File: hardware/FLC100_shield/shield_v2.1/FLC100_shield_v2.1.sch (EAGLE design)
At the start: 55 parts, among them IC2 TSR 1-2450, Q1 2N7000, Q2 2N7000, Q3 2N7000, Q4 2N7000, Q5 2N7000, Q6 2N7000, Q7 2N7000, Q8 2N7000, Q9 2N7000, X1 RJ45, X2 RJ11, X3 CLOUD SENSOR, X4 MEGA2560, X5 HUMIDITY

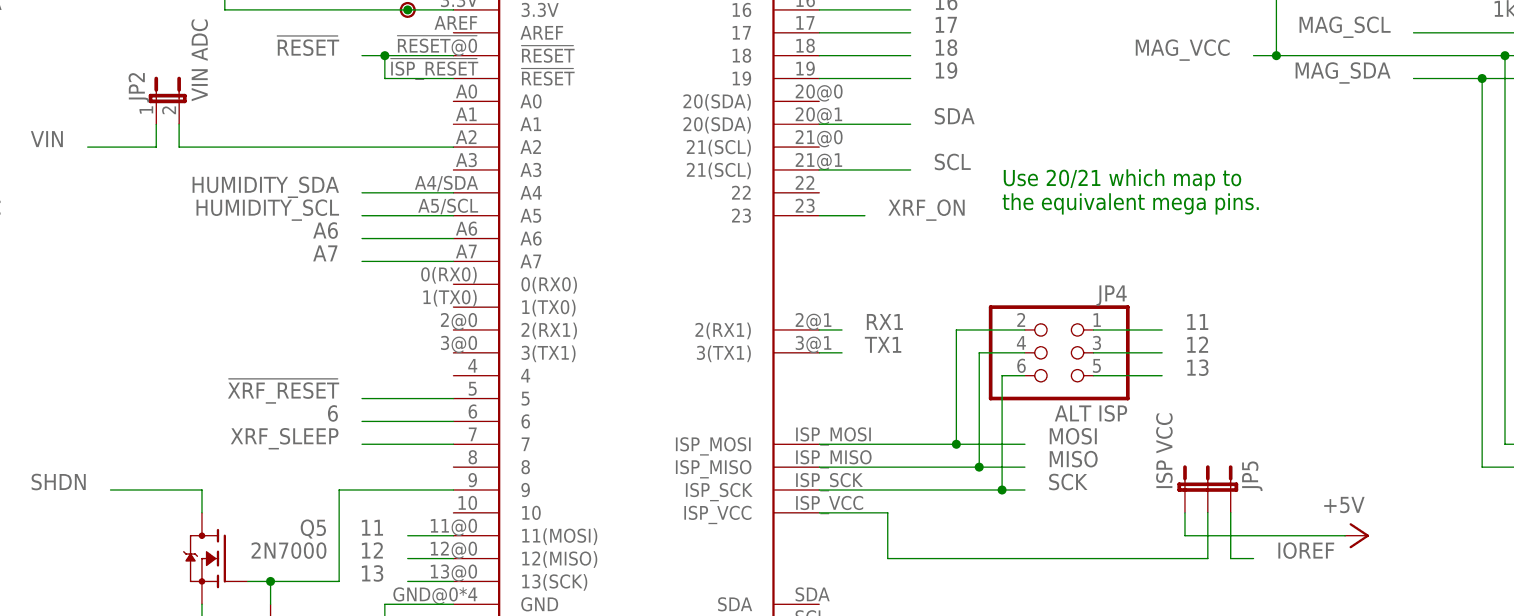
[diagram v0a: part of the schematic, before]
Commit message: Remove unused XRF nets
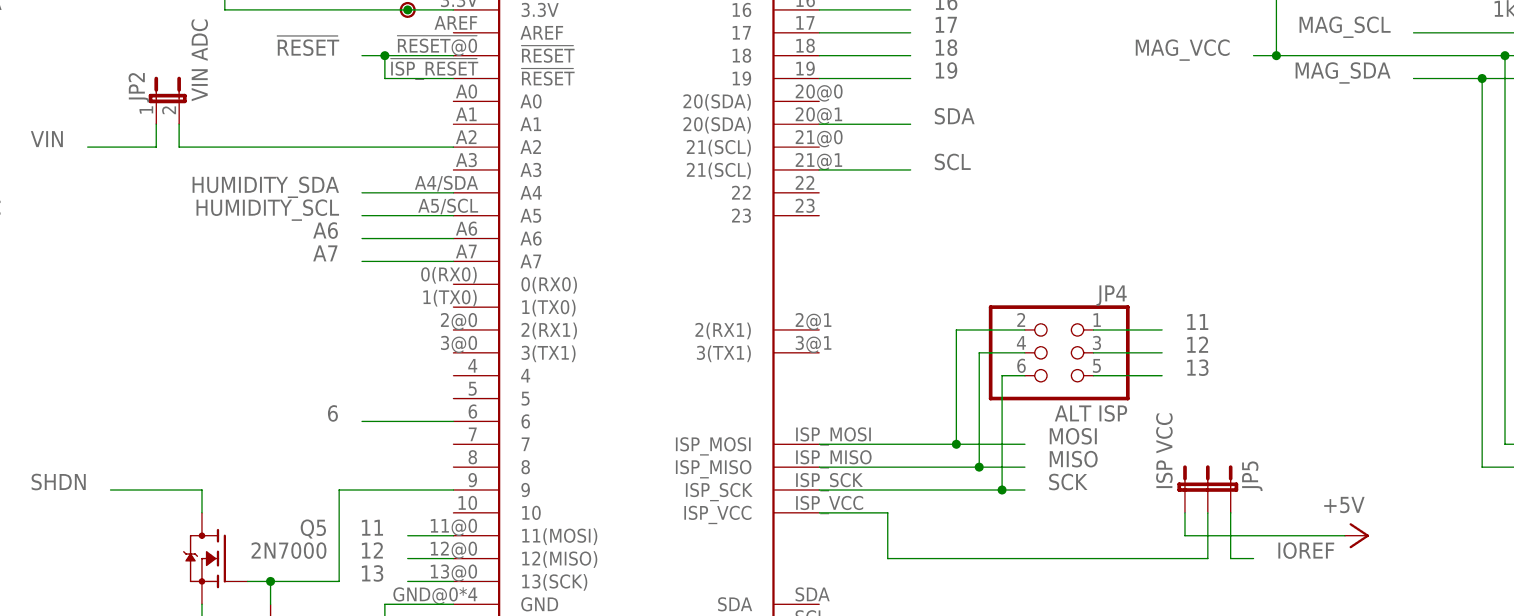
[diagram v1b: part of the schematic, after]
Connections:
- removed net !XRF_RESET: U$4.5
- removed net RX1: U$4.2(RX1)@1
- removed net TX1: U$4.3(TX1)@1
- removed net XRF_ON: U$4.23
- removed net XRF_SLEEP: U$4.7
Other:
- note removed: "Use 20/21 which map to the equivalent mega pins."
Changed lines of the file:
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@@
 <text x="327.406" y="14.732" size="2.54" layer="94">2.1</text>
 <text x="329.946" y="4.572" size="2.54" layer="94">Steve Marple</text>
-<text x="231.14" y="208.28" size="1.778" layer="91" align="top-left">Use 20/21 which map to
-the equivalent mega pins.</text>
 <text x="327.66" y="139.7" size="2.54" layer="91">Temperature sensor</text>
 <text x="20.32" y="22.86" size="2.54" layer="91">3V3 boost regulator</text>
@@
 </segment>
 </net>
-<net name="XRF_ON" class="0">
-<segment>
-<pinref part="U$4" gate="G$1" pin="23"/>
-<wire x1="210.82" y1="203.2" x2="215.9" y2="203.2" width="0.1524" layer="91"/>
-<label x="218.44" y="203.2" size="1.778" layer="95"/>
-</segment>
-</net>
 <net name="!RESET" class="0">
 <segment>
@@
 <wire x1="149.86" y1="160.02" x2="149.86" y2="162.56" width="0.1524" layer="91"/>
 <pinref part="U$4" gate="G$1" pin="9"/>
-</segment>
-</net>
-<net name="!XRF_RESET" class="0">
-<segment>
-<wire x1="170.18" y1="182.88" x2="160.02" y2="182.88" width="0.1524" layer="91"/>
-<label x="157.48" y="182.88" size="1.778" layer="95" rot="MR0"/>
-<pinref part="U$4" gate="G$1" pin="5"/>
-</segment>
-</net>
-<net name="XRF_SLEEP" class="0">
-<segment>
-<wire x1="170.18" y1="177.8" x2="160.02" y2="177.8" width="0.1524" layer="91"/>
-<label x="157.48" y="177.8" size="1.778" layer="95" rot="MR0"/>
-<pinref part="U$4" gate="G$1" pin="7"/>
 </segment>
 </net>
@@
 </segment>
 </net>
-<net name="RX1" class="0">
-<segment>
-<pinref part="U$4" gate="G$1" pin="2(RX1)@1"/>
-<wire x1="210.82" y1="190.5" x2="213.36" y2="190.5" width="0.1524" layer="91"/>
-<label x="215.9" y="190.5" size="1.778" layer="95"/>
-</segment>
-</net>
-<net name="TX1" class="0">
-<segment>
-<pinref part="U$4" gate="G$1" pin="3(TX1)@1"/>
-<wire x1="210.82" y1="187.96" x2="213.36" y2="187.96" width="0.1524" layer="91"/>
-<label x="215.9" y="187.96" size="1.778" layer="95"/>
-</segment>
-</net>
